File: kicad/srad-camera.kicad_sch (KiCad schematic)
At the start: 25 parts, among them J1 SWD, J2 USB_C_Receptacle_USB2.0_14P, J3 Conn_01x02, SW1 RESET, SW2 USER, U1 STM32F407VETx, Y1 Crystal_GND24

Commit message: Fix schematic
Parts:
- removed C10, C11, C12, C13, C14, C4, C5, C6, C7, C8, C9: C, symbol Device:C
- removed C15, C16: 2.2µF, Capacitor_SMD:C_0805_2012Metric, symbol Device:C
- removed R2: R, symbol Device:R
- removed SW2: USER, symbol Switch:SW_Push
- removed U1: STM32F407VETx, Package_QFP:LQFP-100_14x14mm_P0.5mm, symbol MCU_ST_STM32F4:STM32F407VETx
- added C10, C11, C12, C13, C14, C19, C6, C7, C8, C9: 100nf, symbol Device:C_Small
- added C15, C4, C5: 100uf, symbol Device:C_Small
- added C16, C17: 2.2uf, symbol Device:C_Small
- added C18: C, symbol Device:C_Small
- added D1: B5819W, symbol Device:D_Schottky_Small
- added F1: 500mA, symbol Device:Fuse_Small
- added FB1: 100 Ohm @ 100MHz, symbol Device:FerriteBead_Small
- added IMU: LSM6DS3, Module:Adafruit_Feather_M0_Wifi_WithMountingHoles, symbol Sensor_Motion:LSM6DS3
- added MCU: STM32F405RGT6, Package_QFP:LQFP-64_10x10mm_P0.5mm, symbol MCU_ST_STM32F4:STM32F405RGTx
- added R2: R, symbol Device:R_Small
- added R3: 220 Ohm, symbol Device:R_Small
- added R4, R5: 10 kOhm, symbol Device:R_Small
- added SW3: USER, symbol Switch:SW_Push
- added U2: AMS1117-3.3, Package_TO_SOT_SMD:SOT-223-3_TabPin2, symbol Regulator_Linear:AMS1117-3.3
- C1, C2: value C -> 12pf; symbol Device:C -> Device:C_Small
- C3: symbol Device:C -> Device:C_Small
- HSE: renamed from Y1; value Crystal_GND24 -> 25MHz
- R1: symbol Device:R -> Device:R_Small
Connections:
- net GND is gone; now on net +3V3: C1.2, C2.2, C3.1, J1.GND (Pin_9)
- net +3.3V: now also MCU.19 (VDD), MCU.32 (VDD), MCU.48 (VDD), MCU.64 (VDD), R2.1
- net NRST: now reaches J1.RST (Pin_10), R1.2, SW1.2
- net NRST: now also MCU.7 (NRST)
- net +3V3: now reaches HSE.2
- net +3V3: now also HSE.4, C10.1, C10.2, C11.1, C11.2, C12.1, C12.2, C13.1, C13.2, C14.2, C15.1, C15.2, C16.1, C17.1, C18.1, C19.2, C4.2, C5.1, C5.2, C6.1, C6.2, C7.1, C7.2, C8.1, C8.2, C9.1, C9.2, IMU.2 (SDX), IMU.3 (SCX), MCU.12 (VSSA), MCU.18 (VSS), MCU.63 (VSS), R4.2, R5.2, U2.1 (GND), U2.2 (VO); no longer C2.1
- net at C1.1: now also HSE.3, R3.1; no longer HSE.4
- net ?: now reaches J1.SWCLK (Pin_4)
- net ?: now also J1.SWDIO (Pin_2), J1.SWO (Pin_6), IMU.1 (SDO/SA0), IMU.12 (CS), IMU.13 (SCL), IMU.14 (SDA), IMU.4 (INT1)
- net HSE_IN: now reaches HSE.1
- net HSE_IN: now also C2.1, MCU.5 (PH0)
- new net: C16.2, MCU.31 (VCAP_1)
- new net: C17.2, MCU.47 (VCAP_2)
- new net: C4.1, FB1.2, U2.3 (VI)
- new net: C18.2, SW3.1
- new net: C14.1, IMU.5 (VDDIO)
- new net: IMU.6 (GND), IMU.7 (GND)
- new net: C19.1, IMU.8 (VDD)
- new net: D1.1 (K), F1.1
- new net: F1.2, FB1.1
- new net +BATT: MCU.1 (VBAT)
- new net BOOT0: MCU.60 (BOOT0), R4.1
- new net BOOT1: MCU.28 (PB2), R5.1
- new net HSE_OUT: MCU.6 (PH1), R3.2
- new net PA0: R2.2, SW3.2
- new net VCC: D1.2 (A)
- no-connect marks 2 -> 1
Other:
- removed sheet Untitled Sheet
- note added: "Input Voltage Regulator"
- moved on the sheet: C1, C2, C3, HSE, J2, J3, R1, SW1

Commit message: Wired IMU and USBC, add schematics for RK3566
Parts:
- removed MCU: STM32F405RGT6, Package_QFP:LQFP-64_10x10mm_P0.5mm, symbol MCU_ST_STM32F4:STM32F405RGTx
- added C20: 10uF, symbol Device:C_Small
- added C323: 10uF 10V, Capacitor_SMD:C_0603_1608Metric, symbol Device:C
- added C324: 1uF, Capacitor_SMD:C_0402_1005Metric, symbol Device:C
- added C325, C326: 100nF 5%, Capacitor_SMD:C_0201_0603Metric, symbol Device:C
- added D10, D9: D_TVS <1uF, symbol Device:D_TVS_Small
- added D2 (x2), D27, D3, D4, D5, D6, D7: TVS Vr3.3 Vb4, Resistor_SMD:R_0201_0603Metric, symbol Device:D_TVS
- added D8: SMAJ5.0A, Diode_SMD:D_SMA, symbol Diode:SMAJ5.0A
- added FB2, FB3: FerriteBead_Small, symbol Device:FerriteBead_Small
- added MICRO_SD1: TF-01A, TF-01A:TF-01A, symbol TF-01A:TF-01A
- added Q5: FDN340P, Package_TO_SOT_SMD:SOT-23, symbol Transistor_FET:FDN340P
- added R10, R11: 22 Ohm, symbol Device:R_Small
- added R117: 100M, Resistor_SMD:R_0603_1608Metric, symbol Device:R
- added R118: 10k, Resistor_SMD:R_0603_1608Metric, symbol Device:R
- added R12: 1 MOhm, symbol Device:R_Small
- added R15, R16, R17, R18, R19, R20, R21: 33 5%, Resistor_SMD:R_0402_1005Metric, symbol Device:R
- added R6, R7: 10kOhm, symbol Device:R_Small
- added R8, R9: 5.1kOhm, symbol Device:R_Small
- added U1: STM32U575RGT6, Package_QFP:LQFP-64_10x10mm_P0.5mm, symbol MCU_ST_STM32U5:STM32U575RGTx
- added U? (x8): RK3566, BGA-565_L15.5-W14.4-P0.40_RK3566_1, symbol RK35661_RK3566-altium-import:root_0_RK3566_
- C14, C19: value 100nf -> 100nF
- C17: value 2.2uf -> 0.1uF
- J2: value USB_C_Receptacle_USB2.0_14P -> USB_C_PORT; symbol Connector:USB_C_Receptacle_USB2.0_14P -> Connector:USB_C_Receptacle_USB2.0_16P
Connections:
- net +3.3V: now also U1.19 (VDD), U1.32 (VDD), U1.64 (VDD)
- net +3V3: now also C16.2, IMU.1 (SDO/SA0), IMU.6 (GND), IMU.7 (GND), J2.A1 (GND), J2.A12 (GND), J2.B1 (GND), J2.B12 (GND), C20.1, C323.1, C324.2, C325.1, D10.1 (A1), D2.1 (A1), D2.1 (A1), D27.2 (A2), D3.1 (A1), D4.1 (A1), D5.1 (A1), D6.1 (A1), D7.1 (A1), D8.2 (A2), D9.1 (A1), FB2.2, MICRO_SD1.6 (VSS), MICRO_SD1.MP1 (SHIELD), MICRO_SD1.MP2 (SHIELD), MICRO_SD1.MP3 (SHIELD), MICRO_SD1.MP4 (SHIELD), R12.2, R8.2, R9.1, U1.12 (VSSA), U1.18 (VSS), U1.31 (VSS), U1.47 (VSS), U1.63 (VSS); no longer C16.1
- net +BATT: now also U1.1 (VBAT)
- net ?: no longer IMU.1 (SDO/SA0), IMU.12 (CS), IMU.13 (SCL), IMU.14 (SDA), IMU.4 (INT1)
- net BOOT1: now also U1.28 (PB2)
- net HSE_IN: now also U1.5 (PH0)
- net HSE_OUT: now also U1.6 (PH1)
- net NRST: now also U1.7 (NRST)
- net VBUS_USB_5V: now reaches C17.2
- net VBUS_USB_5V: now also C20.2, FB3.1
- net VDDIO_IMU: now reaches C14.1, IMU.5 (VDDIO)
- net VDDIO_IMU: now also IMU.12 (CS), R6.1, R7.1
- net VDD_IMU: now reaches C19.1, IMU.8 (VDD)
- net INT2_IMU: now reaches IMU.9 (INT2)
- net at J2.A4 (VBUS), J2.A9 (VBUS), J2.B4 (VBUS)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: now also D8.1 (A1), FB3.2
- net at J2.A5 (CC1): now also R9.2
- net at J2.A6 (D+): now also J2.B6 (D+), D9.2 (A2), R11.1
- net at J2.A7 (D-): now also J2.B7 (D-), D10.2 (A2), R10.2
- net at J2.B5 (CC2): now also R8.1
- net at J2.S1 (SHIELD): now also FB2.1, R12.1
- new net: D5.2 (A2), MICRO_SD1.1 (DAT2), R19.2
- new net: D7.2 (A2), MICRO_SD1.CD1 (CD), R21.1
- new net: D6.2 (A2), MICRO_SD1.2 (CD/DAT3), R20.2
- new net: D3.2 (A2), MICRO_SD1.7 (DAT0), R17.2
- new net: C323.2, C324.1, C325.2, D27.1 (A1), MICRO_SD1.4 (VDD), Q5.3 (D)
- new net: C326.1, Q5.1 (G), R117.1, R118.2
- new net: C16.1, U1.30 (VCAP)
- new net: D2.2 (A2), MICRO_SD1.5 (CLK), R15.2
- new net: D2.2 (A2), MICRO_SD1.3 (CMD), R16.2
- new net: D4.2 (A2), MICRO_SD1.8 (DAT1), R18.2
- new net INT1_IMU: IMU.4 (INT1)
- new net SCL_IMU: IMU.13 (SCL), R6.2
- new net SDA_IMU: IMU.14 (SDA), R7.2
- new net SDMMC0_CLK: R15.1
- new net SDMMC0_CMD: R16.1
- new net SDMMC0_D0: R17.1
- new net SDMMC0_D1: R18.1
- new net SDMMC0_D2: R19.1
- new net SDMMC0_D3: R20.1
- new net SDMMC0_DET_L: R21.2
- new net SDMMC0_PWR: R118.1
- new net USB_DM: R10.1
- new net USB_DP: R11.2
- new net VCC_3V3: C326.2, Q5.2 (S), R117.2
- no-connect marks 1 -> 4
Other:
- note added: "I2C 0x6A"
- note added: "Input Voltage Regulator (OUTDATED)"
- note added: "LSM6DS3 IMU"
- note added: "USBC 2.0 PORT"
- note removed: "Input Voltage Regulator"
- moved on the sheet: C10, C11, C12, C13, C14, C15, C16, C19, C4, C5, C6, C7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

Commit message: Split schematic to subsheets; wire PMIC, IMU & USB OTG
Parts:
- removed C10, C11, C12, C13, C6, C7, C8, C9: 100nf, symbol Device:C_Small
- removed C14, C19: 100nF, symbol Device:C_Small
- removed C15, C5: 100uf, symbol Device:C_Small
- removed C16: 2.2uf, symbol Device:C_Small
- removed C17: 0.1uF, symbol Device:C_Small
- removed C18: C, symbol Device:C_Small
- removed C20: 10uF, symbol Device:C_Small
- removed C323: 10uF 10V, Capacitor_SMD:C_0603_1608Metric, symbol Device:C
- removed C324: 1uF, Capacitor_SMD:C_0402_1005Metric, symbol Device:C
- removed C325, C326: 100nF 5%, Capacitor_SMD:C_0201_0603Metric, symbol Device:C
- removed D1: B5819W, symbol Device:D_Schottky_Small
- removed D10, D9: D_TVS <1uF, symbol Device:D_TVS_Small
- removed D2 (x2), D27, D3, D4, D5, D6, D7: TVS Vr3.3 Vb4, Resistor_SMD:R_0201_0603Metric, symbol Device:D_TVS
- removed D8: SMAJ5.0A, Diode_SMD:D_SMA, symbol Diode:SMAJ5.0A
- removed F1: 500mA, symbol Device:Fuse_Small
- removed FB1: 100 Ohm @ 100MHz, symbol Device:FerriteBead_Small
- removed FB2, FB3: FerriteBead_Small, symbol Device:FerriteBead_Small
- removed HSE: 25MHz, symbol Device:Crystal_GND24
- removed IMU: LSM6DS3, Module:Adafruit_Feather_M0_Wifi_WithMountingHoles, symbol Sensor_Motion:LSM6DS3
- removed J1: SWD, symbol Connector_Generic:Conn_02x05_Odd_Even
- removed J2: USB_C_PORT, symbol Connector:USB_C_Receptacle_USB2.0_16P
- removed MICRO_SD1: TF-01A, TF-01A:TF-01A, symbol TF-01A:TF-01A
- removed Q5: FDN340P, Package_TO_SOT_SMD:SOT-23, symbol Transistor_FET:FDN340P
- removed R10, R11: 22 Ohm, symbol Device:R_Small
- removed R117: 100M, Resistor_SMD:R_0603_1608Metric, symbol Device:R
- removed R118: 10k, Resistor_SMD:R_0603_1608Metric, symbol Device:R
- removed R12: 1 MOhm, symbol Device:R_Small
- removed R15, R16, R17, R18, R19, R20, R21: 33 5%, Resistor_SMD:R_0402_1005Metric, symbol Device:R
- removed R2: R, symbol Device:R_Small
- removed R3: 220 Ohm, symbol Device:R_Small
- removed R4, R5: 10 kOhm, symbol Device:R_Small
- removed R6, R7: 10kOhm, symbol Device:R_Small
- removed R8, R9: 5.1kOhm, symbol Device:R_Small
- removed SW1: RESET, symbol Switch:SW_Push
- removed SW3: USER, symbol Switch:SW_Push
- removed U1: STM32U575RGT6, Package_QFP:LQFP-64_10x10mm_P0.5mm, symbol MCU_ST_STM32U5:STM32U575RGTx
- removed U2: AMS1117-3.3, Package_TO_SOT_SMD:SOT-223-3_TabPin2, symbol Regulator_Linear:AMS1117-3.3
- removed U? (x8): RK3566, BGA-565_L15.5-W14.4-P0.40_RK3566_1, symbol RK35661_RK3566-altium-import:root_0_RK3566_
- added FPC1: 1.0K-ES-15PWB, srad-camera-footprints:FPC-SMD_15P-P1.00_HDGC_1.0K-ES-15PWB, symbol 1.0K-ES-15PWB1_1.0K-ES-15PWB-altium-import:root_0_1.0K-ES-15PWB_
- added L1: 3.9uH, symbol Device:L_Small
- added SW1: PWRON, symbol Switch:SW_SPST
- added U1: AP63203WU, Package_TO_SOT_SMD:TSOT-23-6, symbol Regulator_Switching:AP63203WU
- C1: value 12pf -> 100nF
- C2: value 12pf -> 10uF
- C3: value C -> 2x22uF
- C4: value 100uf -> 100nF
- JST1: renamed from J3; value Conn_01x02 -> XAP-02V-1
- R1: value R -> 22 kOhm
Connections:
- net HSE_IN is gone; now on an unnamed net: C2.1
- net NRST is gone; now on net GND: R1.2
- net RK809-5 PMIC/PWRON: now reaches C4.1
- net RK809-5 PMIC/PWRON: now also SW1.2 (B)
- net at JST1.1 (Pin_1): now also U1.2 (EN), U1.3 (IN)
- net GND: now reaches JST1.2 (Pin_2)
- net GND: now also C2.2, C3.1, C4.2, SW1.1 (A), U1.4 (GND)
- net VSYS_3V3: now reaches C3.2
- net VSYS_3V3: now also L1.2, U1.1 (FB)
- net at C1.1: now also U1.6 (BST)
- net +3.3V renamed RK809-5 PMIC/EXT_EN
- removed net +3V3: C1.2, C2.2, C3.1, C4.2
- new net: C1.2, L1.1, U1.5 (SW)
- no-connect marks 4 -> 0
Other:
- added sheet LSM6DSRTR IMU (subsheets/imu.kicad_sch)
- added sheet MT41K256 RAM (subsheets/ddr3l.kicad_sch)
- added sheet MicroSD Port (page 6) (subsheets/microsd.kicad_sch)
- added sheet RK3566 SoC (subsheets/rk-soc.kicad_sch)
- added sheet RK809-5 PMIC (subsheets/pmic.kicad_sch)
- added sheet STM32U575RGT6 MCU (subsheets/stm32.kicad_sch)
- added sheet USBC 2.0 Port (subsheets/usbc.kicad_sch)
- note removed: "I2C 0x6A"
- note removed: "Input Voltage Regulator (OUTDATED)"
- note removed: "LSM6DS3 IMU"
- note removed: "USBC 2.0 PORT"

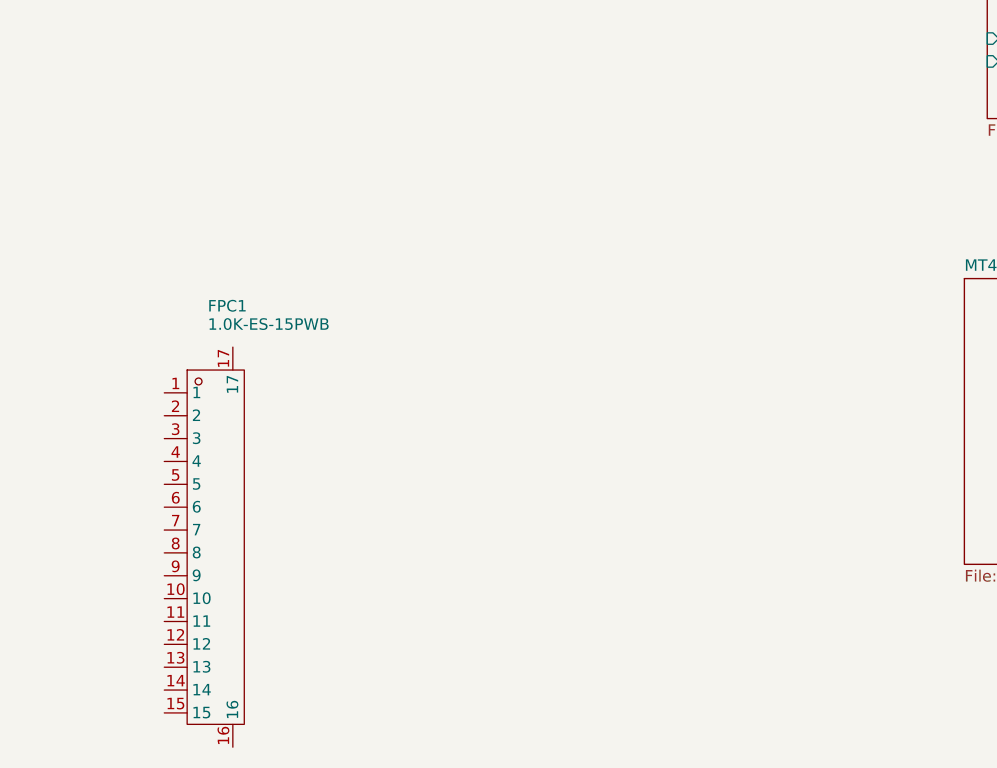
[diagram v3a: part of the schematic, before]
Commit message: Switch to 22pin FPC conn
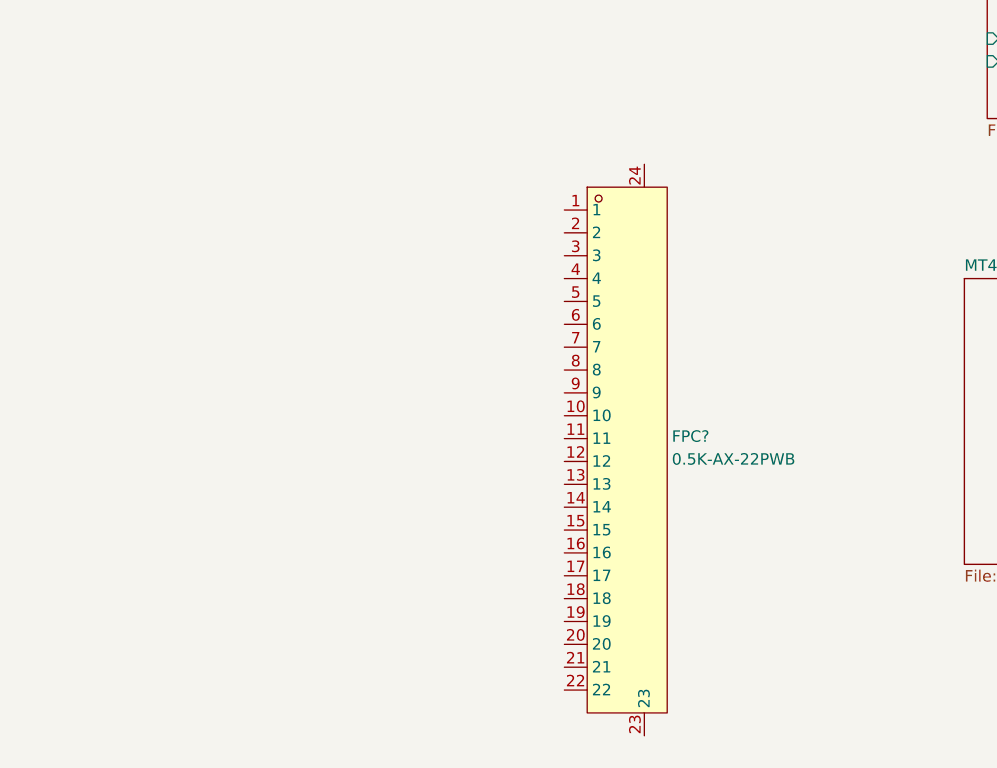
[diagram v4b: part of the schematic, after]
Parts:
- removed FPC1: 1.0K-ES-15PWB, srad-camera-footprints:FPC-SMD_15P-P1.00_HDGC_1.0K-ES-15PWB, symbol 1.0K-ES-15PWB1_1.0K-ES-15PWB-altium-import:root_0_1.0K-ES-15PWB_
- added FPC?: 0.5K-AX-22PWB, srad-camera-footprints:FPC-SMD_22P-P0.50_HDGC_0.5K-AX-22PWB, symbol srad-camera-symbols:0.5K-AX-22PWB

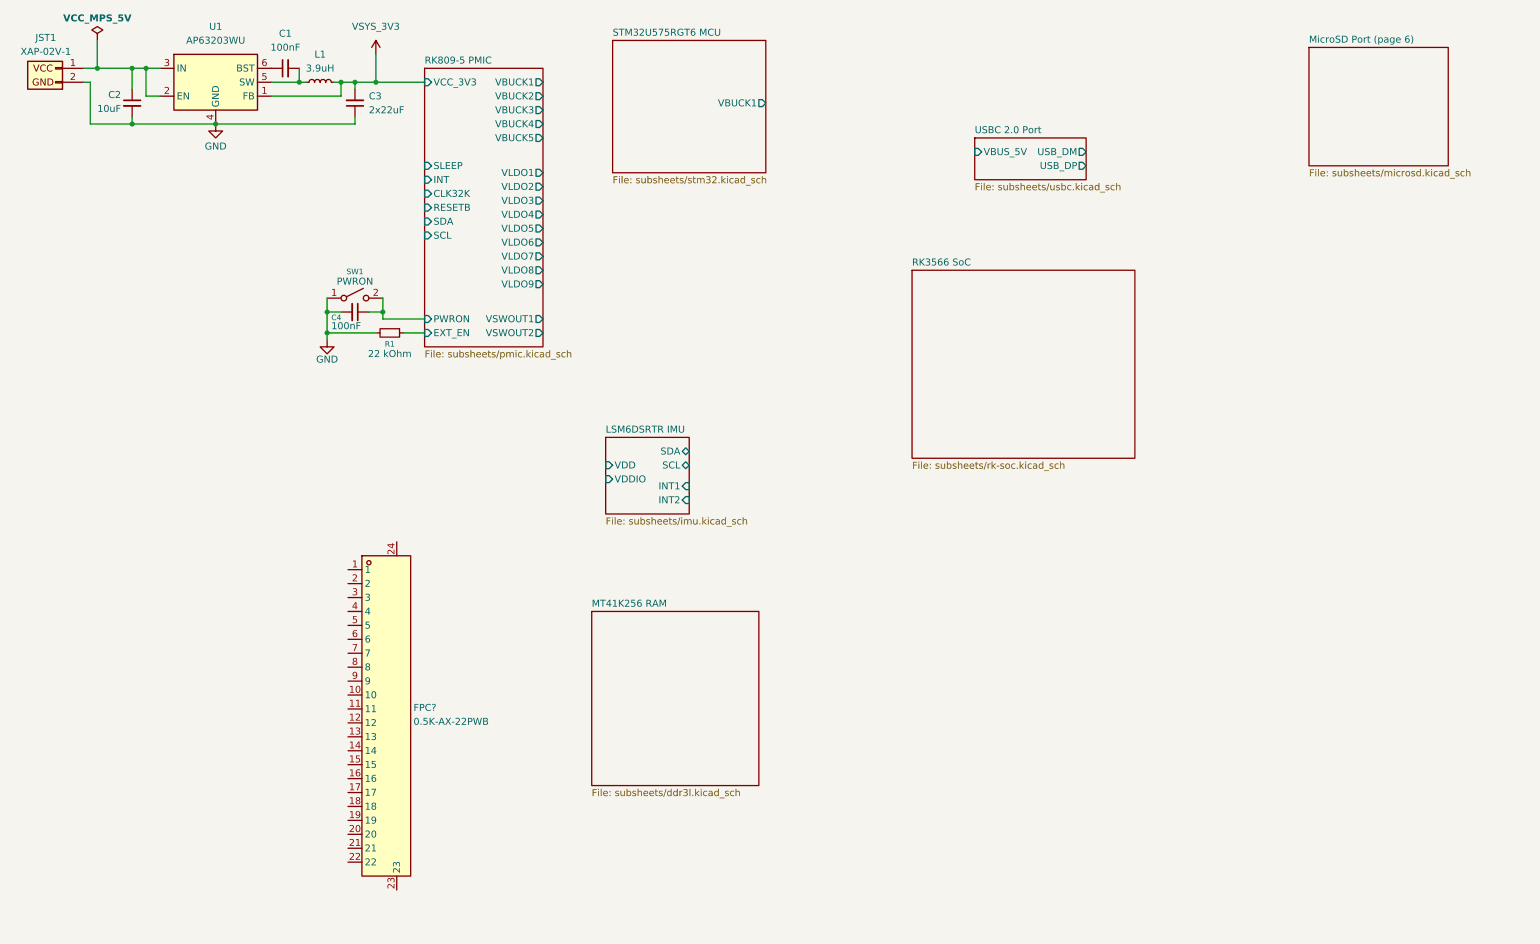
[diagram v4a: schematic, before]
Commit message: Clean up root wiring
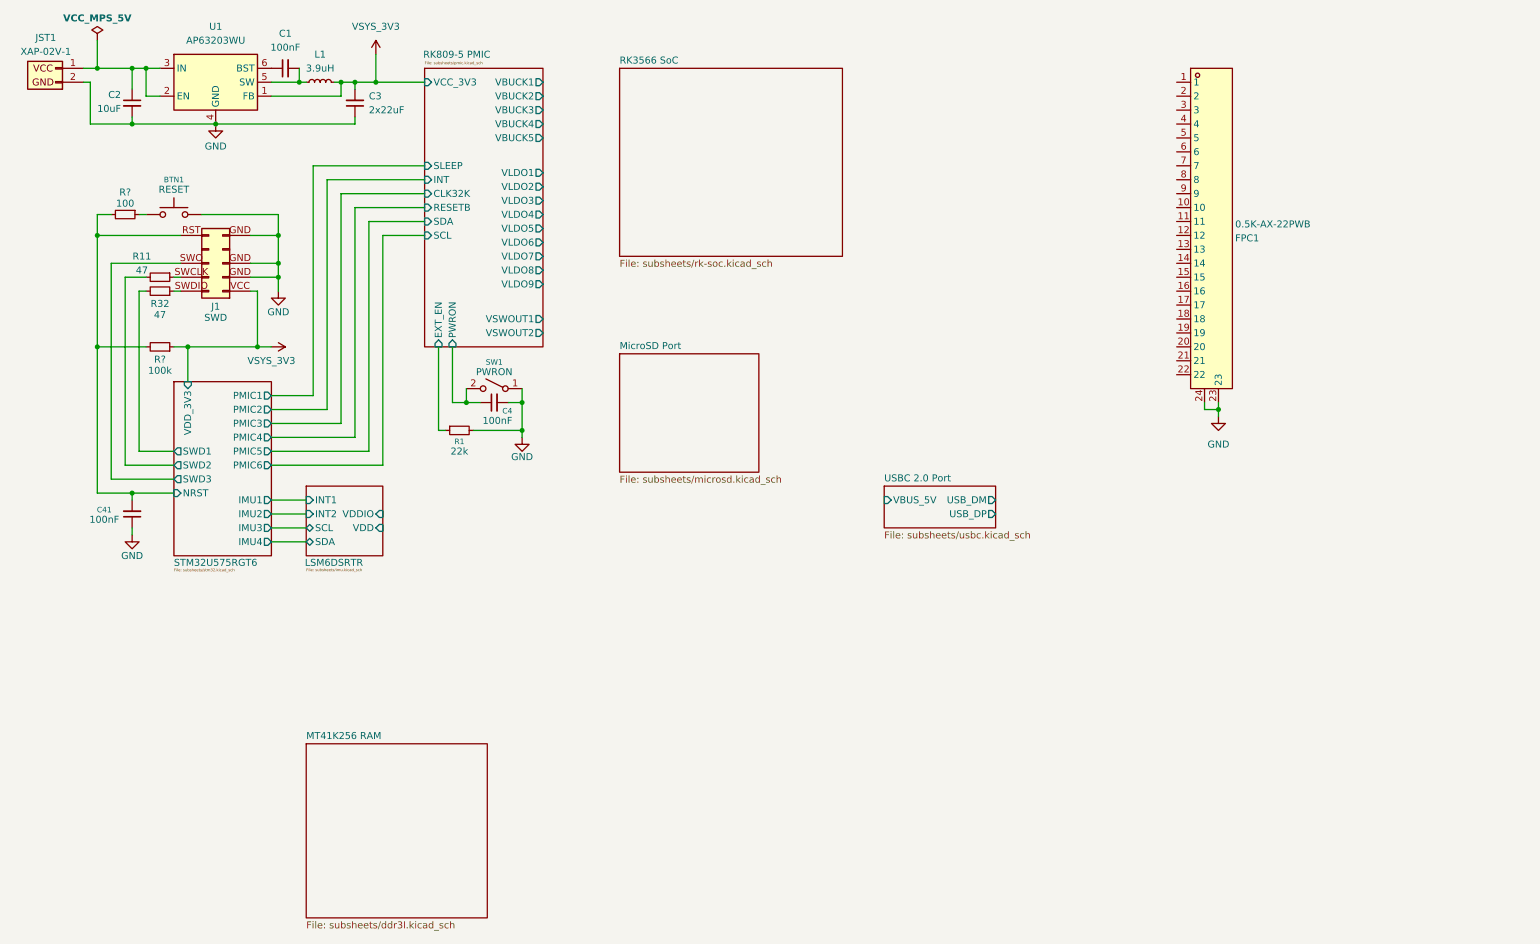
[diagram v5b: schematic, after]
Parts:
- added BTN1: RESET, symbol Switch:SW_Push
- added C41: 100nF, symbol Device:C_Small
- added J1: SWD, symbol Connector_Generic:Conn_02x05_Odd_Even
- added R11, R32: 47, symbol Device:R_Small
- added R?: 100k, symbol Device:R_Small
- added R?: 100, symbol Device:R_Small
- R1: value 22 kOhm -> 22k
- gave numbers to parts that had none: 1
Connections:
- net GND: now also FPC1.23, FPC1.24, BTN1.2, C41.1, J1.GND (Pin_9)
- net VSYS_3V3: now also J1.VCC (Pin_1), R?.1
- new net: BTN1.1, R?.1
- new net: J1.SWCLK (Pin_4), R11.1
- new net: J1.SWDIO (Pin_2), R32.1
- new net STM32U575RGT6/NRST: C41.2, J1.RST (Pin_10), R?.2, R?.2
- new net STM32U575RGT6/SWD1: R32.2
- new net STM32U575RGT6/SWD2: R11.2
- new net STM32U575RGT6/SWD3: J1.SWO (Pin_6)
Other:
- sheet LSM6DSRTR IMU renamed LSM6DSRTR
- sheet MicroSD Port (page 6) renamed MicroSD Port
- sheet STM32U575RGT6 MCU renamed STM32U575RGT6
- sheet STM32U575RGT6 ports: added IMU1, IMU2, IMU3, IMU4, NRST, PMIC1, PMIC2, PMIC3, PMIC4, PMIC5, PMIC6, SWD1, SWD2, SWD3, VDD_3V3; removed VBUCK1
- moved on the sheet: C4, FPC1, R1, SW1
